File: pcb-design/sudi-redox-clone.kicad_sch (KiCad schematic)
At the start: 90 parts, among them J1 AudioJack4, J2 Serial_Out, K1 KEYSW, K10 KEYSW, K11 KEYSW, K12 KEYSW, K13 KEYSW, K14 KEYSW, K15 KEYSW, K16 KEYSW, K17 KEYSW, K18 KEYSW, K19 KEYSW, K2 KEYSW, K20 KEYSW, K21 KEYSW, K22 KEYSW, K23 KEYSW, K24 KEYSW, K25 KEYSW, K26 KEYSW, K27 KEYSW, K28 KEYSW, K29 KEYSW, K3 KEYSW, K30 KEYSW, K31 KEYSW, K32 KEYSW, K33 KEYSW, K34 KEYSW, K35 KEYSW, K36 KEYSW, K37 KEYSW, K38 KEYSW, K39 KEYSW, K4 KEYSW, K40 KEYSW, K41 KEYSW, K42 KEYSW, K5 KEYSW, K6 KEYSW, K7 KEYSW, K8 KEYSW, K9 KEYSW, U1 ProMicro, U2 MCP23017_SP

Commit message: generate gerber and routed board rev 0.1
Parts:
- removed J1: AudioJack4, Connector_Audio:Jack_3.5mm_Ledino_KB3SPRS_Horizontal, symbol Connector_Audio:AudioJack4
- added FID1, FID2, FID3, FID4, FID5, FID6, FID7, FID8, FID9: Fiducial, Fiducial:Fiducial_1mm_Mask3mm, symbol Mechanical:Fiducial
- added H1, H2, H3, H4, H5, H6, H7, H8, H9: MountingHole_Pad, MountingHole:MountingHole_3.2mm_M3_DIN965_Pad, symbol Mechanical:MountingHole_Pad
- added J1: RJ12_LEFT, Connector_RJ:RJ12_Amphenol_54601, symbol Connector:RJ12
- added J3: 0.91 OLED, KiCad-SSD1306-0.91-OLED-4pin-128x32:SSD1306-0.91-OLED-4pin-128x32, symbol Connector:Conn_01x04_Socket
- added J4: RJ12_RIGHT, Connector_RJ:RJ12_Amphenol_54601, symbol Connector:RJ12
- D1, D10, D11, D12, D13, D14, D15, D16, D17, D18, D19, D2, D20, D21, D22, D23, D24, D25, D26, D27, D28, D29, D3, D30, D31, D32, D33, D34, D35, D36, D37, D38, D39, D4, D40, D41, D42, D5, D6, D7, D8, D9: footprint Diode_SMD:D_0805_2012Metric -> canadian_footprints:D_SOD123_axial-dual
- K2, K3, K4: footprint canadian_footprints:Mx_Alps_100-dualside -> canadian_footprints:Mx_Alps_150-dualsided
- R1, R2: footprint (none) -> Resistor_SMD:R_1206_3216Metric
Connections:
- net +5V: now also U2.16 (A1), U2.17 (A2), U2.18 (~{RESET}), J1.6, J3.2 (Pin_2), J4.6
- net GND: now also U2.15 (A0), H2.1, H9.1, J1.2, J3.1 (Pin_1), J4.2
- net SCL: now also J1.4, J3.3 (Pin_3), J4.4
- net SDA: now also J1.5, J3.4 (Pin_4), J4.5
- net Tx: now also J1.3, J4.3
- no-connect marks 7 -> 11
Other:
- note added: "Hardware Address Decoder 110 -> 0x06"
- note added: "Key Matrix"
- note added: "MCP23017"
- note added: "OLED 0.91'"
- note added: "Promicro"
- note added: "RJ12 Female Conn"
- note added: "Serial Out (TX)"
- moved on the sheet: D1, D10, D11, D12, D13, D14, D15, D16, D17, D18, D19, D2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

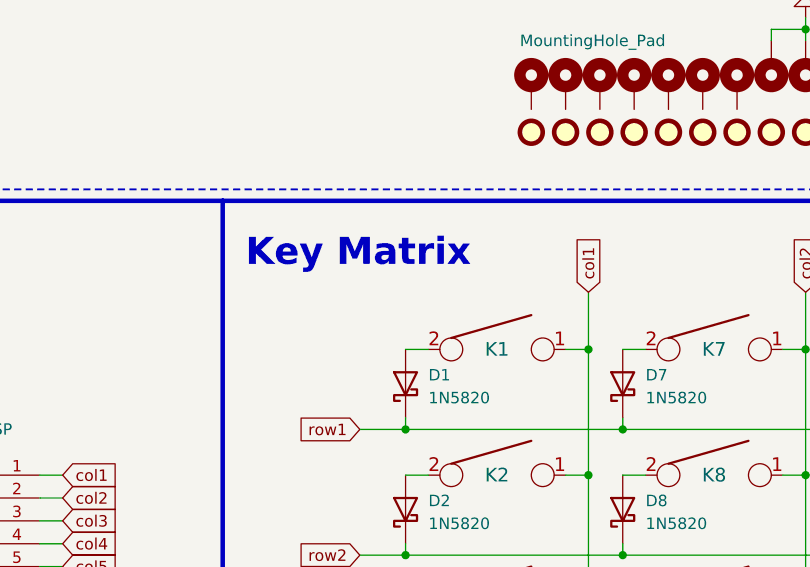
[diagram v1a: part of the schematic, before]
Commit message: generate dxf file - 1
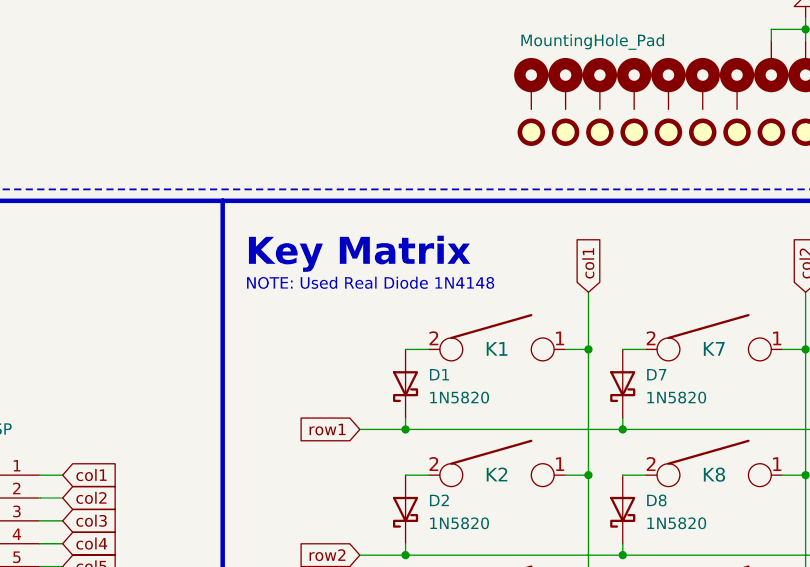
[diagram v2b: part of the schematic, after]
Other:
- note added: "NOTE: Used Real Diode 1N4148"
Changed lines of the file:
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@@
     (title "SUDI - Ergonomic Split Keyboard")
     (date "2023-11-04")
-    (rev "0.1")
+    (rev "0.2")
     (company "AHAH_TERROR")
     (comment 1 "Made With Love By AH")
@@
     (effects (font (size 3 3) bold) (justify left bottom))
   )
+  (text "NOTE: Used Real Diode 1N4148" (at 96.52 74.93 0)
+    (effects (font (face "Hack Nerd Font Mono") (size 1.27 1.27)) (justify left bottom))
+  )
   (text "Serial Out (TX)" (at 83.82 171.45 0)

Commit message: [jumat 28 juni 2024] sudi v2 started
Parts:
- added D43: WS2812B, LED_SMD:LED_WS2812B_PLCC4_5.0x5.0mm_P3.2mm, symbol LED:WS2812B
- added U3: STM32F103RBTx, Package_QFP:LQFP-64_10x10mm_P0.5mm, symbol MCU_ST_STM32F1:STM32F103RBTx
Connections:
- new net: U3.18 (VSS), U3.31 (VSS), U3.47 (VSS), U3.63 (VSS)

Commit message: updatee
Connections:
- no-connect marks 11 -> 18
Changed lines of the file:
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@@
 	(title_block
 		(title "SUDI - Ergonomic Split Keyboard")
-		(date "2024-06-28")
+		(date "2024-07-01")
 		(rev "1")
 		(company "AHAH_TERROR")
@@
 	)
 	(no_connect
+		(at 128.27 54.61)
+	)
+	(no_connect
 		(at 38.1 110.49)
 	)
@@
 	)
 	(no_connect
+		(at 147.32 54.61)
+	)
+	(no_connect
+		(at 139.7 54.61)
+	)
+	(no_connect
+		(at 143.51 54.61)
+	)
+	(no_connect
+		(at 151.13 54.61)
+	)
+	(no_connect
 		(at 229.87 33.02)
 	)
 	(no_connect
+		(at 132.08 54.61)
+	)
+	(no_connect
 		(at 204.47 30.48)
 	)
@@
 	)
 	(no_connect
+		(at 135.89 54.61)
+	)
+	(no_connect
 		(at 73.66 133.35)
 	)
@@
 		)
 	)
-	(text_box "SUDI - Split Keyboard \nSUDI is my custom split keyboard based on redox, it will designed\nwith 75%+ keyboard layout (84 key with 42 each side).\nuse promicro for main MCU and MCP23017 for 16bit bidirectional I/O \nexpantion"
+	(text_box "SUDI - Split Keyboard \nSUDI is my custom split keyboard based on redox, it will designed\nwith 75%+ keyboard layout (84 key with 42 each side).\nuse promicro for main MCU and MCP23017 for 16bit bidirectional I/O \nexpantion\nkailh hot swap"
 		(exclude_from_sim no)
 		(at 12.7 12.7 0)

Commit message: add several component to schematic
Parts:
- added C1, C4, C5, C6, C7, C8: 100nF, symbol Device:C
- added C10, C9: 22pF, symbol Device:C
- added C2, C3: 10uF/5V, symbol Device:C_Polarized
- added D44, D45, D46, D47, D48, D49, D50: WS2812B, LED_SMD:LED_WS2812B_PLCC4_5.0x5.0mm_P3.2mm, symbol LED:WS2812B
- added FB1: 60R@100Mhz, symbol Device:FerriteBead
- added J5: USB_C, symbol Connector:USB_C_Receptacle_USB2.0_14P
- added J6: V_BAT, symbol Connector_Generic:Conn_01x02
- added J7: Conn_ARM_JTAG_SWD_10, symbol Connector:Conn_ARM_JTAG_SWD_10
- added R3, R4: 5K1, Resistor_SMD:R_1206_3216Metric, symbol Device:R_US
- added SW1: RST, symbol Switch:SW_Push
- added U4: AMS1117-3.3, Package_TO_SOT_SMD:SOT-223-3_TabPin2, symbol Regulator_Linear:AMS1117-3.3
- added Y1: 8MHz, symbol Device:Crystal
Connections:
- net +5V: now also D43.1 (VDD), C2.1, D44.1 (VDD), D45.1 (VDD), D46.1 (VDD), D47.1 (VDD), D48.1 (VDD), D49.1 (VDD), D50.1 (VDD), FB1.2, U4.3 (VI)
- net GND: now also D43.3 (VSS), U3.12 (VSSA), U3.18 (VSS), U3.31 (VSS), U3.47 (VSS), U3.63 (VSS), C1.2, C10.1, C2.2, C3.2, C4.2, C5.2, C6.2, C7.2, C8.2, C9.1, D44.3 (VSS), D45.3 (VSS), D46.3 (VSS), D47.3 (VSS), D48.3 (VSS), D49.3 (VSS), D50.3 (VSS), J5.A1 (GND), J5.A12 (GND), J5.B1 (GND), J5.B12 (GND), J5.S1 (SHIELD), J6.2 (Pin_2), R3.2, R4.2, SW1.1, U4.1 (GND)
- net +BATT: now reaches U3.1 (VBAT)
- net +BATT: now also C7.1, J6.1 (Pin_1)
- net +3.3V: now reaches U3.13 (VDDA)
- net +3.3V: now also U3.19 (VDD), U3.32 (VDD), U3.48 (VDD), U3.64 (VDD), C1.1, C3.1, C4.1, C5.1, C6.1, U4.2 (VO)
- net I2C2_SCL: now reaches U3.29 (PB10)
- net I2C2_SDA: now reaches U3.30 (PB11)
- net USBD-: now reaches U3.44 (PA11)
- net USBD-: now also J5.A7 (D-), J5.B7 (D-)
- net USBD+: now reaches U3.45 (PA12)
- net USBD+: now also J5.A6 (D+), J5.B6 (D+)
- net at U3.5 (PD0): now also C10.2, Y1.1
- net USART1_TX: now reaches U3.58 (PB6)
- net USART1_RX: now reaches U3.59 (PB7)
- net at U3.6 (PD1): now also C9.2, Y1.2
- net NRST: now reaches U3.7 (NRST)
- net NRST: now also C8.1, SW1.2
- net at D43.2 (DOUT): now also D44.4 (DIN)
- new net: D45.2 (DOUT), D46.4 (DIN)
- new net: D44.2 (DOUT), D45.4 (DIN)
- new net: J5.A5 (CC1), R3.1
- new net: D47.2 (DOUT), D48.4 (DIN)
- new net: D46.2 (DOUT), D47.4 (DIN)
- new net: J7.3 (GND), J7.5 (GND)
- new net: D48.2 (DOUT), D49.4 (DIN)
- new net: D49.2 (DOUT), D50.4 (DIN)
- new net: J5.B5 (CC2), R4.1
- new net: FB1.1, J5.A4 (VBUS), J5.A9 (VBUS), J5.B4 (VBUS), J5.B9 (VBUS)
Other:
- note added: "ADD USB B Backup"
- note added: "Chrystal Reference From Datasheet https://www.st.com/resource/en/application_note/an2586-getting-started-with-stm32f10xxx-hardware-development-stmicroelectronics.pdf"
- note added: "RJ12 Female Conn Change To Correct Footprint"
- note added: "STM32F103RBT6"
- note added: "Serial Out (TX) Direct connect to RGB LED"
- note added: "USB Type C Reference https://dubiouscreations.com/2021/04/06/designing-with-usb-c-lessons-learned/ Filter Reference https://www.reddit.com/r/PrintedCircuitBoard/comments/12bfhsv/mini_design_review_vbus_protection/"
- note removed: "Promicro"
- note removed: "RJ12 Female Conn"
- note removed: "Serial Out (TX)"
- moved on the sheet: J1, J2, J4, U1, U3

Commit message: add nordic design Reference
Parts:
- added U5: nRF51x22-QFxx, Package_DFN_QFN:QFN-48-1EP_6x6mm_P0.4mm_EP4.6x4.6mm, symbol MCU_Nordic:nRF51x22-QFxx
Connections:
- new net: U5.1 (VDD), U5.12 (VDD)
- new net: U5.13 (VSS), U5.33 (VSS), U5.34 (VSS)
- new net: U5.35 (AVDD), U5.36 (AVDD)
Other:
- note added: "V2 TODO make it wireless with NRF51822 add BMS to System (TP4056) make receiver and transmitter with NRF"
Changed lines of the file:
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@@
+		)
+	)
+	(text "V2 TODO \nmake it wireless with NRF51822\nadd BMS to System (TP4056)\nmake receiver and transmitter with NRF \n\n"
+		(exclude_from_sim no)
+		(at 378.206 -95.25 0)
+		(effects
+			(font
+				(size 12.7 12.7)
+			)
+			(justify left)
 		)
 	)
@@
 					(unit 1)
 				)
+			)
+		)
+	)
+	(symbol
+		(lib_id "MCU_Nordic:nRF51x22-QFxx")
+		(at 439.42 52.07 0)
+		(unit 1)
+		(exclude_from_sim no)
+		(in_bom yes)
+		(on_board yes)
+		(dnp no)
+		(fields_autoplaced yes)
+		(property "Reference" "U5"
+			(at 444.1541 97.79 0)
+			(effects
+				(font
+					(size 1.27 1.27)
+				)
+				(justify left)
+			)
+		)
+		(property "Value" "nRF51x22-QFxx"
+			(at 444.1541 100.33 0)
+			(effects
+				(font
+					(size 1.27 1.27)
+				)
+				(justify left)
+			)
+		)
+		(property "Footprint" "Package_DFN_QFN:QFN-48-1EP_6x6mm_P0.4mm_EP4.6x4.6mm"
+			(at 439.42 52.07 0)
+			(effects
+				(font
+					(size 1.27 1.27)
+				)
+				(hide yes)
+			)
+		)
+		(property "Datasheet" "http://infocenter.nordicsemi.com/pdf/nRF51822_PS_v3.3.pdf"
+			(at 429.26 54.61 0)
+			(effects
+				(font
+					(size 1.27 1.27)
+				)
+				(hide yes)
+			)
+		)
+		(property "Description" "Multiprotocol BLE/2.4GHz Cortex-M0+ SoC"
+			(at 439.42 52.07 0)
+			(effects
+				(font
+					(size 1.27 1.27)
+				)
+				(hide yes)
+			)
+		)
+		(pin "20"
+		)
+		(pin "14"
+		)
+		(pin "17"
+		)
+		(pin "28"
+		)
+		(pin "3"
+		)
+		(pin "2"
+		)
+		(pin "23"
+		)
+		(pin "32"
+		)
+		(pin "35"
+		)
+		(pin "11"
+		)
+		(pin "37"
+		)
+		(pin "41"
+		)
+		(pin "10"
+		)
+		(pin "15"
+		)
+		(pin "42"
+		)
+		(pin "4"
+		)
+		(pin "44"
+		)
+		(pin "13"
+		)
+		(pin "30"
+		)
+		(pin "21"
+		)
+		(pin "31"
+		)
+		(pin "16"
+		)
+		(pin "43"
+		)
+		(pin "46"
+		)
+		(pin "19"
+		)
+		(pin "49"
+		)
+		(pin "7"
+		)
+		(pin "40"
+		)
+		(pin "38"
+		)
+		(pin "39"
+		)
+		(pin "24"
+		)
+		(pin "26"
+		)
+		(pin "48"
+		)
+		(pin "33"
+		)
+		(pin "36"
+		)
+		(pin "47"
+		)
+		(pin "34"
+		)
+		(pin "18"
+		)
+		(pin "6"
+		)
+		(pin "9"
+		)
+		(pin "12"
+		)
+		(pin "1"
+		)
+		(pin "29"
+		)
+		(pin "5"
+		)
+		(pin "27"
+		)
+		(pin "25"
+		)
+		(pin "8"
+		)
+		(pin "22"
+		)
+		(pin "45"
+		)
+		(instances
+			(project "sudi-redox-clone"
+				(path "/5bbd2338-13ff-49b0-9f87-5cbfec528c5b"
+					(reference "U5")
+					(unit 1)
+				)

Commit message: [minggu 7 juli 7:27] create receiver schematic
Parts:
- removed C10, C9: 22pF, symbol Device:C
- removed C5, C6, C7: 100nF, symbol Device:C
- removed D10, D11, D12, D16, D17, D18, D22, D23, D24, D28, D29, D30, D34, D35, D36, D37, D38, D39, D4, D40, D41, D42, D5, D6: 1N5820, canadian_footprints:D_SOD123_axial-dual, symbol Diode:1N5820
- removed D49, D50: WS2812B, LED_SMD:LED_WS2812B_PLCC4_5.0x5.0mm_P3.2mm, symbol LED:WS2812B
- removed J6: V_BAT, symbol Connector_Generic:Conn_01x02
- removed K10, K11, K12, K16, K17, K18, K22, K23, K24, K28, K29, K30, K34, K35, K36, K37, K38, K39, K40, K41, K42, K5, K6: KEYSW, canadian_footprints:Mx_Alps_100-dualside, symbol canadian_parts:KEYSW
- removed K4: KEYSW, canadian_footprints:Mx_Alps_150-dualsided, symbol canadian_parts:KEYSW
- removed U1: ProMicro, canadian_footprints:Pro_Micro, symbol ProMicro:ProMicro
- removed U2: MCP23017_SP, Package_DIP:DIP-28_W7.62mm, symbol Interface_Expansion:MCP23017_SP
- removed U3: STM32F103RBTx, Package_QFP:LQFP-64_10x10mm_P0.5mm, symbol MCU_ST_STM32F1:STM32F103RBTx
- removed Y1: 8MHz, symbol Device:Crystal
- added AE1: 2.4GHz, RF_Antenna:Texas_SWRA117D_2.4GHz_Left, symbol Device:Antenna
- added C11, C13, C21: 100nF, symbol Device:C
- added C12: 47nF, symbol Device:C
- added C14: 1nF, symbol Device:C
- added C15: 2.2pF, symbol Device:C
- added C16: 1pF, symbol Device:C
- added C17: 1.5p, symbol Device:C
- added C18: 2.2nF, symbol Device:C
- added C19, C20: 12pF, symbol Device:C
- added D10, D11, D12, D16, D17, D18, D22, D23, D24, D28, D5, D6: WS2812B, LED_SMD:LED_WS2812B_PLCC4_5.0x5.0mm_P3.2mm, symbol LED:WS2812B
- added D4: RED, LED_SMD:LED_0805_2012Metric_Pad1.15x1.40mm_HandSolder, symbol Device:LED
- added J8: BatCon, Connector_PinHeader_2.54mm:PinHeader_1x02_P2.54mm_Horizontal, symbol Connector_Generic:Conn_01x02
- added L1: 10nH, symbol Device:L
- added L2: 4.7nH, symbol Device:L
- added L3: 3.3nH, symbol Device:L
- added R5, R7: 1K, Resistor_SMD:R_1206_3216Metric, symbol Device:R_US
- added R6: 1.2, Resistor_SMD:R_1206_3216Metric, symbol Device:R_US
- added U6: TP4056, Package_SO:SOIC-8-1EP_3.9x4.9mm_P1.27mm_EP2.29x3mm, symbol tp4056:TP4056
- added U8: MCP23017_SS, Package_SO:SSOP-28_5.3x10.2mm_P0.65mm, symbol Interface_Expansion:MCP23017_SS
- added Y2: 16MHz, symbol Device:Crystal
- C1, C4: value 100nF -> 10uF
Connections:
- net +3.3V: now also R1.1, R2.1, U5.1 (VDD), U5.12 (VDD), U5.35 (AVDD), U5.36 (AVDD), C13.1, C14.1, C21.1, U8.9 (VDD); no longer C1.1, C4.1
- net +5V: now also C4.1, D4.2 (A), U6.4 (VCC), U6.8 (CE), U8.16 (A1), U8.17 (A2), U8.18 (~{RESET}); no longer D43.1 (VDD), D44.1 (VDD), D45.1 (VDD), D46.1 (VDD), D47.1 (VDD), D48.1 (VDD), J1.6, J2.1 (Pin_1), J3.2 (Pin_2), J4.6, R1.1, R2.1
- net GND: now also U5.13 (VSS), U5.33 (VSS), U5.34 (VSS), U5.49 (EP), C11.2, C12.2, C13.2, C14.2, C16.2, C17.2, C18.2, C19.1, C20.1, C21.2, D10.3 (VSS), D11.3 (VSS), D12.3 (VSS), D16.3 (VSS), D17.3 (VSS), D18.3 (VSS), D22.3 (VSS), D23.3 (VSS), D24.3 (VSS), D28.3 (VSS), D5.3 (VSS), D6.3 (VSS), J8.2 (Pin_2), R5.1, R6.1, U6.3 (GND), U8.10 (VSS), U8.15 (A0)
- net I2C2_SCL: now also U5.4 (P0.0)
- net I2C2_SDA: now also U5.5 (P0.1)
- net SCL: now also U8.12 (SCK)
- net SDA: now also U8.13 (SDA)
- net USART1_RX: now also U5.7 (P0.3)
- net USART1_TX: now also D43.4 (DIN), U5.6 (P0.2)
- net col1: now also U5.11 (P0.7), U8.1 (GPB0)
- net col2: now also U5.14 (P0.8), U8.2 (GPB1)
- net col3: now also U5.15 (P0.9), U8.3 (GPB2)
- net col4: now also U5.16 (P0.10), U8.4 (GPB3)
- net col5: now also U5.17 (P0.11), U8.5 (GPB4)
- net col6: now also U5.18 (P0.12), U8.6 (GPB5)
- net row1: now also U5.8 (P0.4), U8.21 (GPA0)
- net row2: now also U5.9 (P0.5), U8.22 (GPA1)
- net row3: now also U5.10 (P0.6), U8.23 (GPA2)
- net at U5.24 (SWDCLK): now also R5.2
- net at U5.29 (DEC2): now also C12.1
- net at U5.30 (VDD_PA): now also C18.1, L1.2
- net at U5.31 (ANT1): now also L1.1, L2.2
- net at U5.32 (ANT2): now also C15.1, L2.1
- net at U5.37 (XC1): now also C19.2, Y2.1
- net at U5.38 (XC2): now also C20.2, Y2.2
- net at U5.39 (DEC1): now also C11.1
- net at D48.2 (DOUT): now also D5.4 (DIN)
- new net: D5.2 (DOUT), D6.4 (DIN)
- new net: C1.1, J8.1 (Pin_1), U6.5 (BAT)
- new net: R6.2, U6.2 (PROG)
- new net: R7.1, U6.7 (~{CHRG})
- new net: D17.2 (DOUT), D18.4 (DIN)
- new net: D16.2 (DOUT), D17.4 (DIN)
- new net: D24.2 (DOUT), D28.4 (DIN)
- new net: D23.2 (DOUT), D24.4 (DIN)
- new net: D22.2 (DOUT), D23.4 (DIN)
- new net: D10.2 (DOUT), D11.4 (DIN)
- new net: D10.4 (DIN), D6.2 (DOUT)
- new net: D18.2 (DOUT), D22.4 (DIN)
- new net: D4.1 (K), R7.2
- new net: C15.2, C16.1, L3.2
- new net: AE1.1 (A), C17.1, L3.1
- new net: D12.2 (DOUT), D16.4 (DIN)
- new net: D11.2 (DOUT), D12.4 (DIN)
- new net +3V7: D10.1 (VDD), D11.1 (VDD), D12.1 (VDD), D16.1 (VDD), D17.1 (VDD), D18.1 (VDD), D22.1 (VDD), D23.1 (VDD), D24.1 (VDD), D28.1 (VDD), D43.1 (VDD), D44.1 (VDD), D45.1 (VDD), D46.1 (VDD), D47.1 (VDD), D48.1 (VDD), D5.1 (VDD), D6.1 (VDD), J1.6, J2.1 (Pin_1), J3.2 (Pin_2), J4.6
- no-connect marks 18 -> 22
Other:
- added sheet Receiver (Receiver.kicad_sch)
- note added: "28.2 Master mode pin configuration TWI master are mapped to physical pins according to the configuration specified in the PSELSCL and PSELSDA registers respectively."
- note added: "Ref: Figure 24 NRF51822 Datasheet"
- note added: "V2 TODO make it wireless with NRF51822 add BMS to System (TP4056) make receiver and transmitter with NRF use LUFA with ATMega8 for usb receiver / RECEIVER SCH https://www.fourwalledcubicle.com/files/LUFA/Doc/120219/html/_page__a_v_r8_support.html https://developer.nordicsemi.com/nRF5_SDK/nRF51_SDK_v4.x.x/doc/html/group__ble__sdk__app__hids__keyboard.html"
- note removed: "Chrystal Reference From Datasheet https://www.st.com/resource/en/application_note/an2586-getting-started-with-stm32f10xxx-hardware-development-stmicroelectronics.pdf"
- note removed: "V2 TODO make it wireless with NRF51822 add BMS to System (TP4056) make receiver and transmitter with NRF"
- title: SUDI - Ergonomic Split Keyboard -> SUDI - Main Schematic
- moved on the sheet: D43, D44, D45, D46, D47, D48, J2, J7

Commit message: [minggu 7 juli 8:55] cleaning schematic layout
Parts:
- removed D32, D33: 1N5820, canadian_footprints:D_SOD123_axial-dual, symbol Diode:1N5820
- removed J2: Serial_Out, Connector_PinHeader_2.54mm:PinHeader_1x03_P2.54mm_Horizontal, symbol Connector:Conn_01x03_Pin
- removed J3: 0.91 OLED, KiCad-SSD1306-0.91-OLED-4pin-128x32:SSD1306-0.91-OLED-4pin-128x32, symbol Connector:Conn_01x04_Socket
- removed J4: RJ12_RIGHT, Connector_RJ:RJ12_Amphenol_54601, symbol Connector:RJ12
- removed K19, K20, K21, K25, K26, K27, K31, K32, K33: KEYSW, canadian_footprints:Mx_Alps_100-dualside, symbol canadian_parts:KEYSW
- added D29, D30: 1N5820, canadian_footprints:D_SOD123_axial-dual, symbol Diode:1N5820
- added J2: 0.91 OLED, KiCad-SSD1306-0.91-OLED-4pin-128x32:SSD1306-0.91-OLED-4pin-128x32, symbol Connector:Conn_01x04_Socket
- added J3: RJ12_RIGHT, Connector_RJ:RJ12_Amphenol_54601, symbol Connector:RJ12
- added K10, K11, K12, K16, K17, K18, K4, K5, K6: KEYSW, canadian_footprints:Mx_Alps_100-dualside, symbol canadian_parts:KEYSW
- J7: value Conn_ARM_JTAG_SWD_10 -> ARMJTAG
- R6: value 1.2 -> 1K
- R7: value 1K -> 1.2
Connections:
- net +3.3V: now also J7.1 (VTref)
- net +3V7: now also J2.2 (Pin_2), J3.6
- net +5V: now also C1.1; no longer C4.1
- net GND: now also H8.1, J7.3 (GND), J7.5 (GND), J7.9 (GNDDetect), R7.1, J2.1 (Pin_1), J3.2; no longer H2.1, R6.1
- net SCL: now also J2.3 (Pin_3), J3.4
- net SDA: now also J2.4 (Pin_4), J3.5
- net Tx: now also J3.3
- net col2: now also K4.1, K5.1, K6.1; no longer K7.1, K8.1, K9.1
- net col3: now also K7.1, K8.1, K9.1; no longer K13.1, K14.1, K15.1
- net col4: now also K10.1, K11.1, K12.1
- net col5: now also K13.1, K14.1, K15.1
- net col6: now also K16.1, K17.1, K18.1
- net row1: now also D29.1 (K); no longer D31.1 (K)
- net row2: now also D30.1 (K)
- net row3: now also D31.1 (K)
- net at D27.2 (A): now also K15.2
- net at K7.2: now also D13.2 (A); no longer D7.2 (A)
- net at J8.1 (Pin_1), U6.5 (BAT): now also C4.1; no longer C1.1
- net at D20.2 (A): now also K11.2
- net SWDIO: now reaches U5.23 (SWDIO/~{RST})
- net SWDIO: now also J7.2 (SWDIO/TMS)
- net SWCLK: now reaches R5.2, U5.24 (SWDCLK)
- net SWCLK: now also J7.4 (SWCLK/TCK)
- net at U6.2 (PROG): now also R7.2; no longer R6.2
- net at U6.7 (~{CHRG}): now also R6.1; no longer R7.1
- net at D14.2 (A): now also K8.2; no longer K14.2
- net at K13.2: now also D25.2 (A); no longer D13.2 (A)
- net at D9.2 (A): now also K6.2; no longer K9.2
- net at D26.2 (A): now also K14.2
- net at D21.2 (A): now also K12.2
- net at D15.2 (A): now also K9.2; no longer K15.2
- net at D4.1 (K): now also R6.2; no longer R7.2
- net at D31.2 (A): now also K18.2
- net at D8.2 (A): now also K5.2; no longer K8.2
- net at D19.2 (A): now also K10.2
- new net: D30.2 (A), K17.2
- new net: D7.2 (A), K4.2
- new net: D29.2 (A), K16.2
- no-connect marks 22 -> 25
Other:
- note removed: "STM32F103RBT6"
- note removed: "Serial Out (TX) Direct connect to RGB LED"
- moved on the sheet: AE1, C11, C12, C13, C14, C15, C16, C17, C18, C19, C2, C20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
